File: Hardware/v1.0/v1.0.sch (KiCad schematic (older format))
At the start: 23 parts, among them J1 Barrel_Jack_Switch, J2 Conn_01x03_Male, K1 G5LE-1, Q2 BC237, U1 LM358, U2 LM555

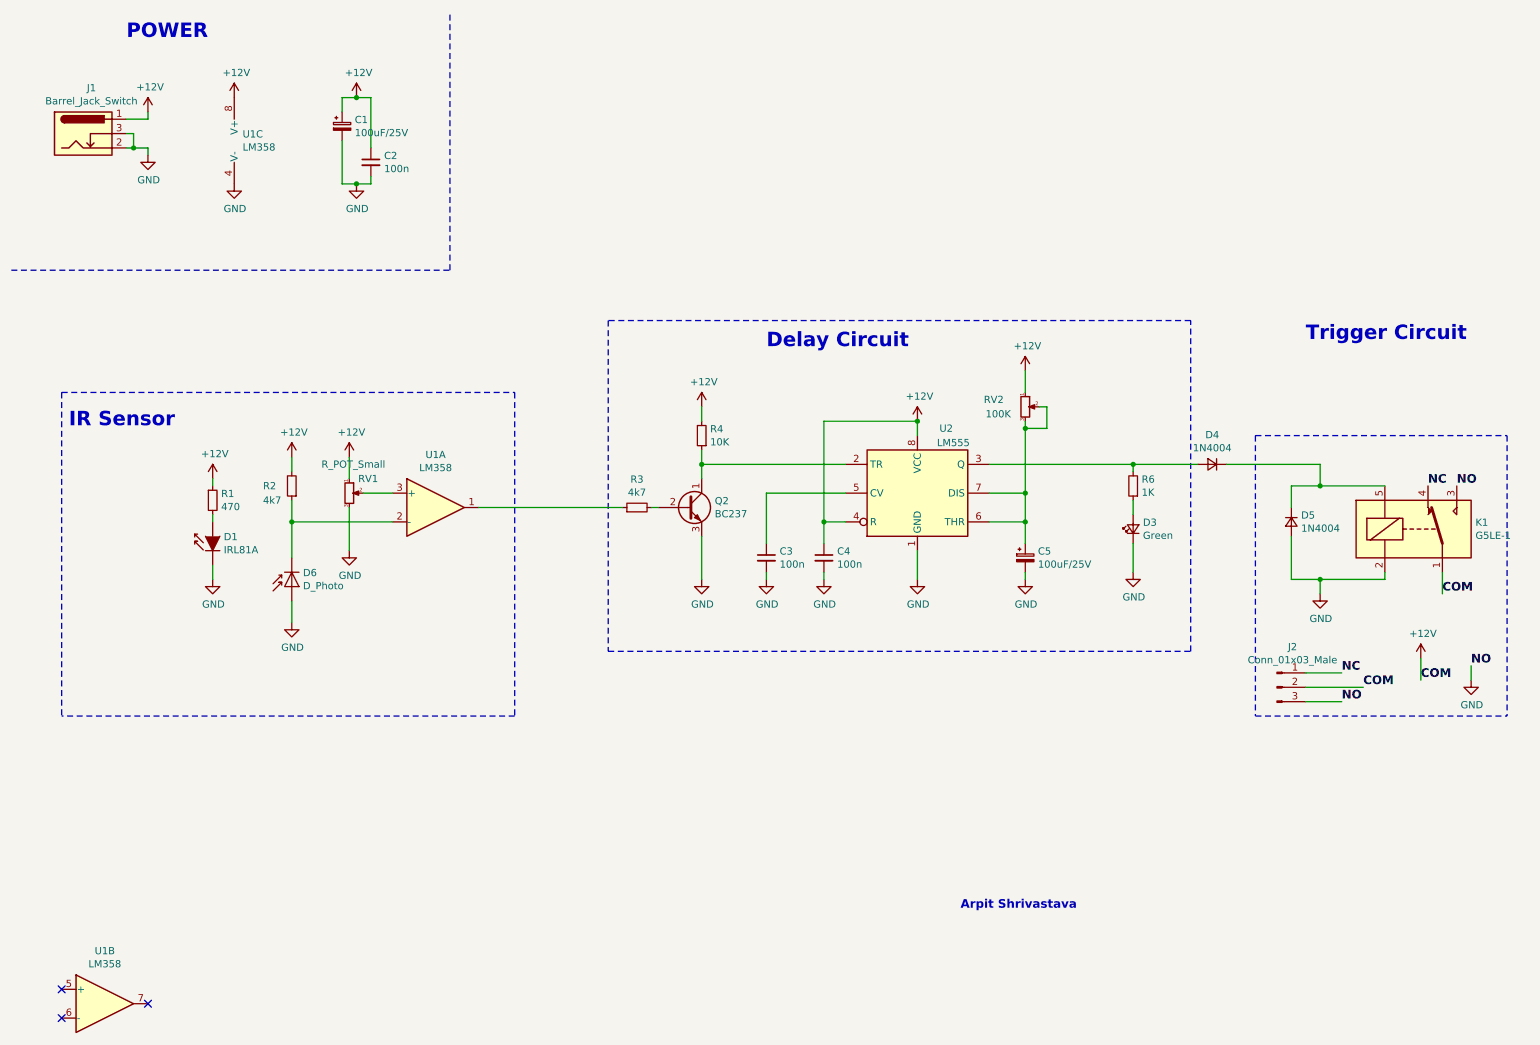
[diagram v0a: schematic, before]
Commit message: design with MOSFET
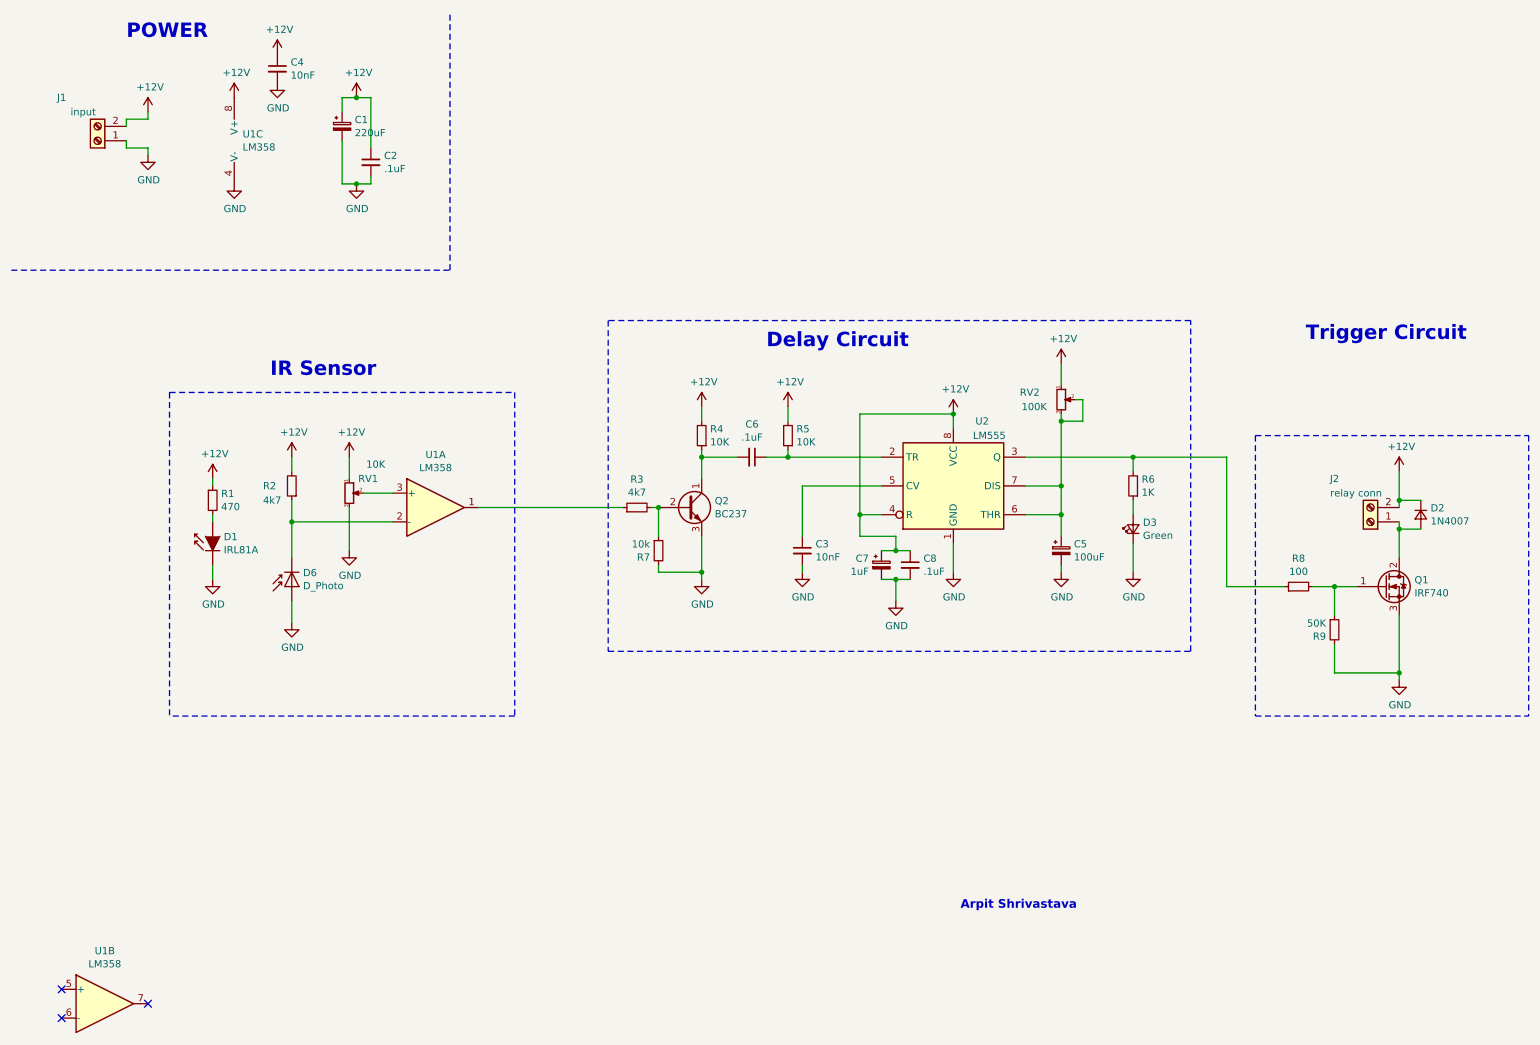
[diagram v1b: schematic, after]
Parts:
- removed D4, D5: 1N4004, Diode_THT:D_A-405_P7.62mm_Horizontal, symbol Device:D_Small
- removed J1: Barrel_Jack_Switch, Connector_BarrelJack:BarrelJack_Horizontal, symbol Connector:Barrel_Jack_Switch
- removed J2: Conn_01x03_Male, TerminalBlock:TerminalBlock_Altech_AK300-2_P5.00mm, symbol Connector:Conn_01x03_Male
- removed K1: G5LE-1, Electromechanical:RELAY-T90, symbol Relay:G5LE-1
- added C6: .1uF, Capacitor_THT:C_Disc_D3.8mm_W2.6mm_P2.50mm, symbol Device:C_Small
- added C7: 1uF, Capacitor_THT:CP_Radial_D5.0mm_P2.50mm, symbol USB_A_Dual:CP_Small
- added C8: .1uF, Capacitor_THT:C_Disc_D3.4mm_W2.1mm_P2.50mm, symbol Device:C_Small
- added D2: 1N4007, Diode_THT:D_DO-41_SOD81_P7.62mm_Horizontal, symbol Device:D_Small
- added J1: input, TerminalBlock_Phoenix:TerminalBlock_Phoenix_MKDS-1,5-2_1x02_P5.00mm_Horizontal, symbol Connector:Screw_Terminal_01x02
- added J2: relay conn, TerminalBlock_Phoenix:TerminalBlock_Phoenix_MKDS-1,5-2_1x02_P5.00mm_Horizontal, symbol Connector:Screw_Terminal_01x02
- added Q1: IRF740, Package_TO_SOT_THT:TO-220-3_Vertical, symbol Transistor_FET:IRF740
- added R5: 10K, Resistor_THT:R_Axial_DIN0207_L6.3mm_D2.5mm_P7.62mm_Horizontal, symbol Device:R_Small
- added R7: 10k, Resistor_THT:R_Axial_DIN0207_L6.3mm_D2.5mm_P7.62mm_Horizontal, symbol Device:R_Small
- added R8: 100, Resistor_THT:R_Axial_DIN0207_L6.3mm_D2.5mm_P7.62mm_Horizontal, symbol Device:R_Small
- added R9: 50K, Resistor_THT:R_Axial_DIN0207_L6.3mm_D2.5mm_P7.62mm_Horizontal, symbol Device:R_Small
- C1: value 100uF/25V -> 220uF
- C2: value 100n -> .1uF
- C3, C4: value 100n -> 10nF
- C5: value 100uF/25V -> 100uF
- Q2: footprint Package_TO_SOT_THT:TO-92_Inline -> Package_TO_SOT_THT:TO-92_HandSolder
- RV1: value R_POT_Small -> 10K
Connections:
- net +12V: now also C7.1, C8.1, D2.1 (K), J1.2 (Pin_2), J2.2 (Pin_2), R5.2
- net GND: now also C7.2, C8.2, J1.1 (Pin_1), Q1.3 (S), R7.2, R9.2
- net at Q2.1 (C), R4.1: now also C6.2; no longer U2.2 (TR)
- net at R6.2, U2.3 (Q): now also R8.1
- net at Q2.2 (B), R3.2: now also R7.1
- new net: C6.1, R5.1, U2.2 (TR)
- new net: Q1.1 (G), R8.2, R9.1
- new net: D2.2 (A), J2.1 (Pin_1), Q1.2 (D)
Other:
- moved on the sheet: C3, C5, RV2, U2
